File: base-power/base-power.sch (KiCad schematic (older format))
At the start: 5 parts

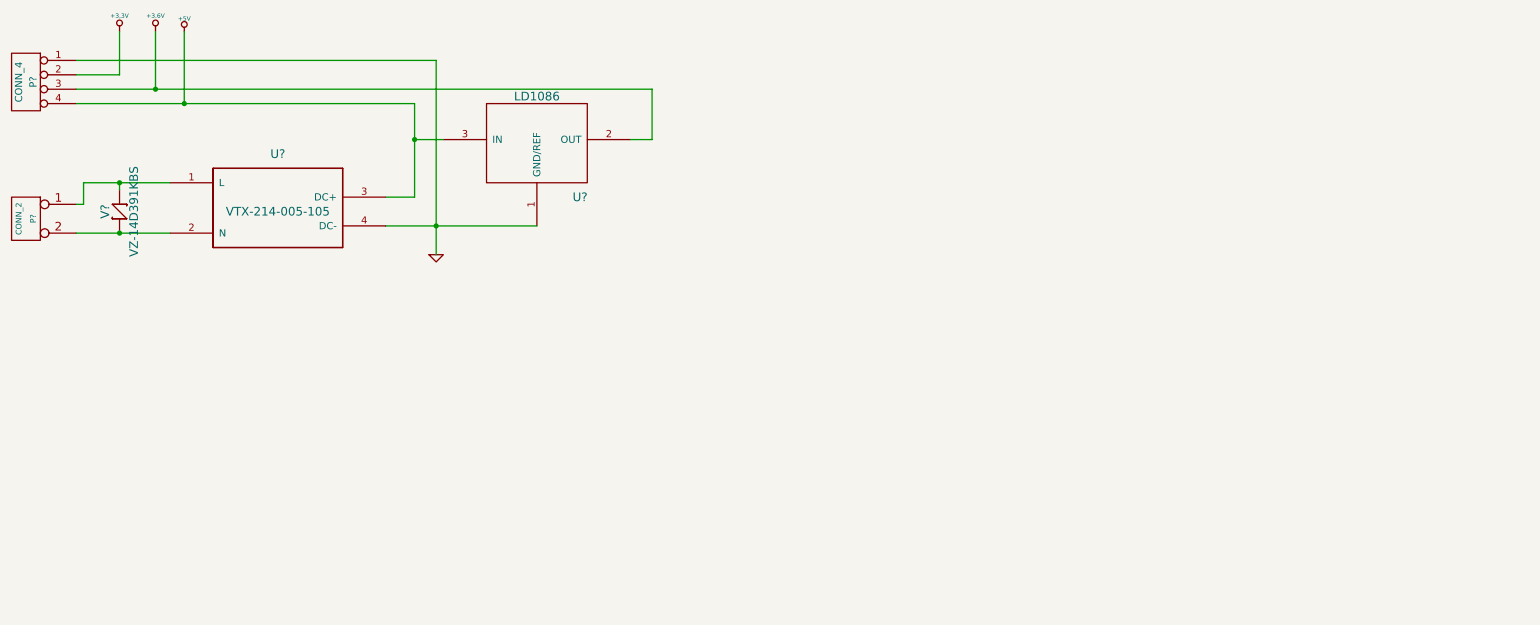
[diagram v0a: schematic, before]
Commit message: Add current sensor, RTC battery, Power protection
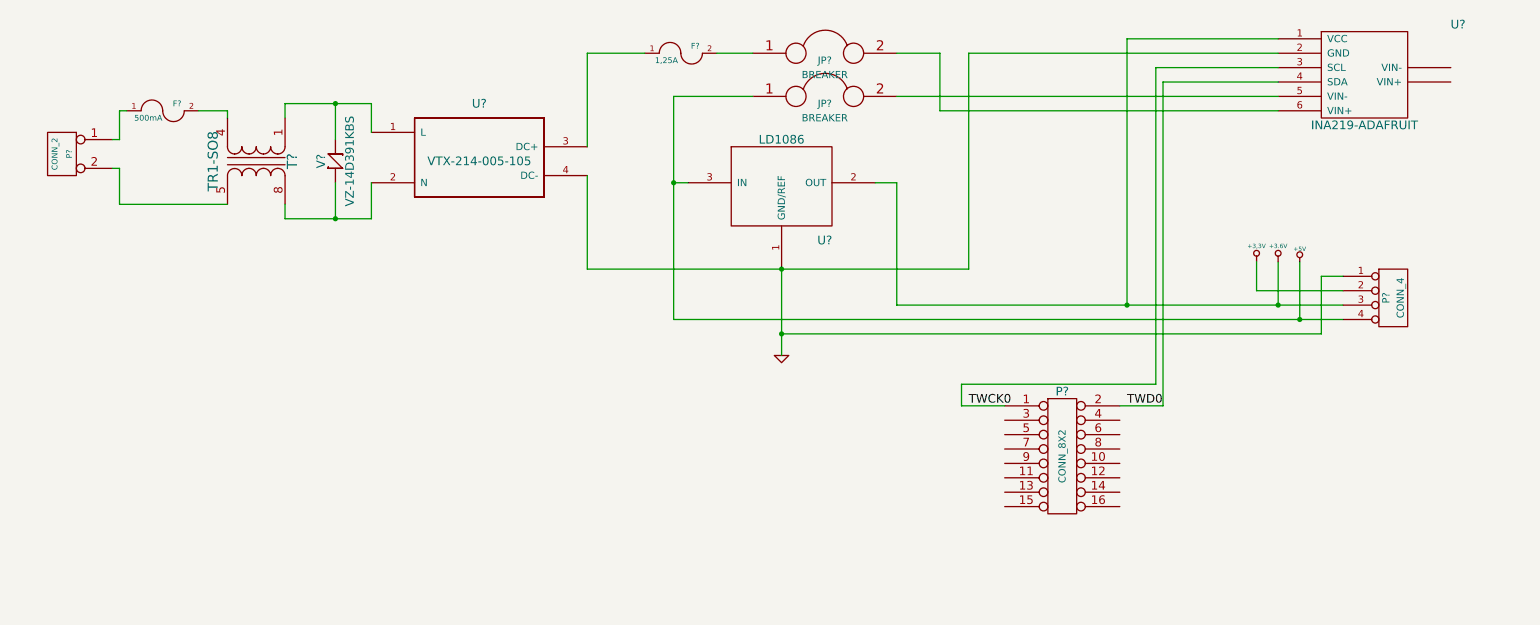
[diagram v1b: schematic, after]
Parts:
- added F?: 500mA, ~, symbol FUSE
- added F?: 1,25A, ~, symbol FUSE
- added JP? (x2): BREAKER, ~, symbol BREAKER
- added P?: CONN_8X2, symbol CONN_8X2
- added T?: TR1-SO8, ~, symbol TR1-SO8
- added U?: INA219-ADAFRUIT, symbol INA219-ADAFRUIT
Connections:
- net +3.6V: now also U?.1 (VCC)
- net +5V: now also JP?.1; no longer U?.3 (DC+)
- net GND: now also U?.2 (GND)
- net at U?.1 (L), V?.1: now also T?.1 (AA); no longer P?.1 (P1)
- net at U?.2 (N), V?.2: now also T?.8 (SB); no longer P?.2 (PM)
- new net: F?.1, P?.1 (P1)
- new net: P?.2 (PM), T?.5 (SA)
- new net: F?.1, U?.3 (DC+)
- new net: F?.2, T?.4 (AB)
- new net: F?.2, JP?.1
- new net: JP?.2, U?.6 (VIN+)
- new net: JP?.2, U?.5 (VIN-)
- new net TWCK0: P?.1, U?.3 (SCL)
- new net TWD0: P?.2, U?.4 (SDA)
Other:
- moved on the sheet: P?, U?, V?

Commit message: Power revision and add ina219 sensor
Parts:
- added P?: AD0, ~, symbol TST
- added P?: AD1, ~, symbol TST
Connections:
- net PD20-AD0: now reaches P?.3
- net PD20-AD0: now also P?.1
- net PD21-AD1: now reaches P?.4
- net PD21-AD1: now also P?.1
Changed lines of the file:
@@
 Sheet 1 1
 Title ""
-Date "18 apr 2017"
+Date "21 apr 2017"
 Rev ""
 Comp ""
@@
 Wire Wire Line
 	8500 3600 8800 3600
+$Comp
+L TST P?
+U 1 1 58FA5824
+P 7100 3500
+F 0 "P?" H 7100 3800 40  0000 C CNN
+F 1 "AD0" H 7100 3750 30  0000 C CNN
+F 2 "~" H 7100 3500 60  0000 C CNN
+F 3 "~" H 7100 3500 60  0000 C CNN
+	1    7100 3500
+	1    0    0    -1
+$EndComp
+Wire Wire Line
+	7100 3700 7100 3500
+Text Label 7250 3700 0    60   ~ 0
+PD20-AD0
+$Comp
+L TST P?
+U 1 1 58FA589A
+P 9150 3500
+F 0 "P?" H 9150 3800 40  0000 C CNN
+F 1 "AD1" H 9150 3750 30  0000 C CNN
+F 2 "~" H 9150 3500 60  0000 C CNN
+F 3 "~" H 9150 3500 60  0000 C CNN
+	1    9150 3500
+	1    0    0    -1
+$EndComp
+Wire Wire Line
+	8500 3700 9150 3700
+Wire Wire Line
+	9150 3700 9150 3500
+Text Label 8550 3700 0    60   ~ 0
+PD21-AD1
+Wire Wire Line
+	7700 3700 7100 3700
 $EndSCHEMATC

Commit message: Fix Power schematics
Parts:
- removed U?: LD1086, ~, symbol LD1086
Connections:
- net +3.3V: now also U?.1 (VCC)
- net +3.6V: no longer names the net of P?.3 (P3)
- net +3.6V: no longer U?.1 (VCC)
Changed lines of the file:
@@
 Sheet 1 1
 Title ""
-Date "21 apr 2017"
+Date "10 jun 2017"
 Rev ""
 Comp ""
@@
 $EndComp
 $Comp
-L +3.6V #PWR?
-U 1 1 58A09B68
-P 9600 2600
-F 0 "#PWR?" H 9600 2560 30  0001 C CNN
-F 1 "+3.6V" H 9600 2710 30  0000 C CNN
-F 2 "~" H 9600 2600 60  0000 C CNN
-F 3 "~" H 9600 2600 60  0000 C CNN
-	1    9600 2600
-	1    0    0    -1
-$EndComp
-$Comp
 L VTX-214-005-105 U?
 U 1 1 58A09B77
@@
 F 3 "" H 6150 3250 60  0000 C CNN
 	1    6150 3250
-	1    0    0    -1
-$EndComp
-$Comp
-L LD1086 U?
-U 1 1 58A098D3
-P 6200 1750
-F 0 "U?" H 6450 1050 60  0000 C CNN
-F 1 "LD1086" H 6150 1750 60  0000 C CNN
-F 2 "~" H 6200 1950 60  0000 C CNN
-F 3 "~" H 6200 1950 60  0000 C CNN
-	1    6200 1750
 	1    0    0    -1
 $EndComp
@@
 	5400 1450 5400 3000
 Wire Wire Line
-	5400 2050 5500 2050
-Wire Wire Line
 	9600 1150 7450 1150
 Wire Wire Line
@@
 Wire Wire Line
 	5400 3000 10050 3000
-Connection ~ 5400 2050
-Wire Wire Line
-	6950 2900 10050 2900
-Wire Wire Line
-	6950 2900 6950 2050
-Wire Wire Line
-	6950 2050 6800 2050
-Wire Wire Line
-	10050 2800 9450 2800
+Wire Wire Line
+	8700 2800 10050 2800
 Wire Wire Line
 	9450 2800 9450 2600
-Wire Wire Line
-	9600 2600 9600 2900
-Connection ~ 9600 2900
 Wire Wire Line
 	9750 2600 9750 3000
@@
 	3050 2050 3050 2300
 Connection ~ 3050 2300
-Wire Wire Line
-	9600 1050 8550 1050
-Wire Wire Line
-	8550 1050 8550 2900
-Connection ~ 8550 2900
 $Comp
 L CONN_8X2 P?
@@
 Wire Wire Line
 	7700 3700 7100 3700
+Wire Wire Line
+	8700 2800 8700 1050
+Wire Wire Line
+	8700 1050 9600 1050
+Connection ~ 9450 2800
 $EndSCHEMATC

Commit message: Add humidity sensors
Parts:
- added M?: HS1101LF-M, symbol HS1101LF-M
- added U?: HIH5030, symbol HIH5030
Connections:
- net labels added: PA10-HS1101-OUT, PA11-HS1101-EN
- wire segments 51 -> 65
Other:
- moved on the sheet: P?
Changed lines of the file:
@@
 Sheet 1 1
 Title ""
-Date "10 jun 2017"
+Date "26 aug 2017"
 Rev ""
 Comp ""
@@
 	8700 2800 10050 2800
 Wire Wire Line
-	9450 2800 9450 2600
-Wire Wire Line
-	9750 2600 9750 3000
+	9450 2600 9450 4350
+Wire Wire Line
+	9750 2600 9750 3600
 Connection ~ 9750 3000
 Wire Wire Line
 	10050 2700 9900 2700
 Wire Wire Line
-	9900 2700 9900 3100
+	9900 2700 9900 4550
 Wire Wire Line
 	9900 3100 6150 3100
@@
 L TST P?
 U 1 1 58FA5824
-P 7100 3500
-F 0 "P?" H 7100 3800 40  0000 C CNN
-F 1 "AD0" H 7100 3750 30  0000 C CNN
-F 2 "~" H 7100 3500 60  0000 C CNN
-F 3 "~" H 7100 3500 60  0000 C CNN
-	1    7100 3500
-	1    0    0    -1
-$EndComp
-Wire Wire Line
-	7100 3700 7100 3500
+P 6800 3500
+F 0 "P?" H 6800 3800 40  0000 C CNN
+F 1 "AD0" H 6800 3750 30  0000 C CNN
+F 2 "~" H 6800 3500 60  0000 C CNN
+F 3 "~" H 6800 3500 60  0000 C CNN
+	1    6800 3500
+	1    0    0    -1
+$EndComp
+Wire Wire Line
+	6800 3500 6800 4450
 Text Label 7250 3700 0    60   ~ 0
 PD20-AD0
@@
 PD21-AD1
 Wire Wire Line
-	7700 3700 7100 3700
+	6800 3700 7700 3700
 Wire Wire Line
 	8700 2800 8700 1050
@@
 	8700 1050 9600 1050
 Connection ~ 9450 2800
+$Comp
+L HS1101LF-M M?
+U 1 1 59A18936
+P 10700 3700
+F 0 "M?" H 10700 4150 60  0000 C CNN
+F 1 "HS1101LF-M" V 10700 3850 39  0000 C CNN
+F 2 "" H 10800 3800 60  0000 C CNN
+F 3 "" H 10800 3800 60  0000 C CNN
+	1    10700 3700
+	0    1    1    0
+$EndComp
+Wire Wire Line
+	9450 3500 10050 3500
+Wire Wire Line
+	9750 3600 10050 3600
+Wire Wire Line
+	7700 3800 7250 3800
+Wire Wire Line
+	7250 3800 7250 4550
+Wire Wire Line
+	7250 4550 9750 4550
+Wire Wire Line
+	9750 4550 9750 3700
+Wire Wire Line
+	9750 3700 10050 3700
+Wire Wire Line
+	9900 3800 10050 3800
+Connection ~ 9900 3100
+Wire Wire Line
+	8500 3800 9150 3800
+Wire Wire Line
+	9150 3800 9150 3900
+Wire Wire Line
+	9150 3900 10050 3900
+Text Label 6900 3800 0    60   ~ 0
+PA11-HS1101-EN
+Text Label 8550 3800 0    60   ~ 0
+PA10-HS1101-OUT
+$Comp
+L HIH5030 U?
+U 1 1 59A18BF8
+P 10750 4450
+F 0 "U?" H 10750 4800 60  0000 C CNN
+F 1 "HIH5030" H 10750 4550 39  0000 C CNN
+F 2 "" H 10750 4450 60  0000 C CNN
+F 3 "" H 10750 4450 60  0000 C CNN
+	1    10750 4450
+	0    1    1    0
+$EndComp
+Wire Wire Line
+	9450 4350 10250 4350
+Connection ~ 9450 3500
+Connection ~ 9900 3800
+Wire Wire Line
+	9900 4550 10250 4550
+Wire Wire Line
+	6800 4450 10250 4450
+Connection ~ 6800 3700
 $EndSCHEMATC
